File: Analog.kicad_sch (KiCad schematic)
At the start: 15 parts, among them J2 Conn_01x02_Socket, J3 Conn_01x02_Socket, U3 MAX98357A, U7 TLV172IDCK

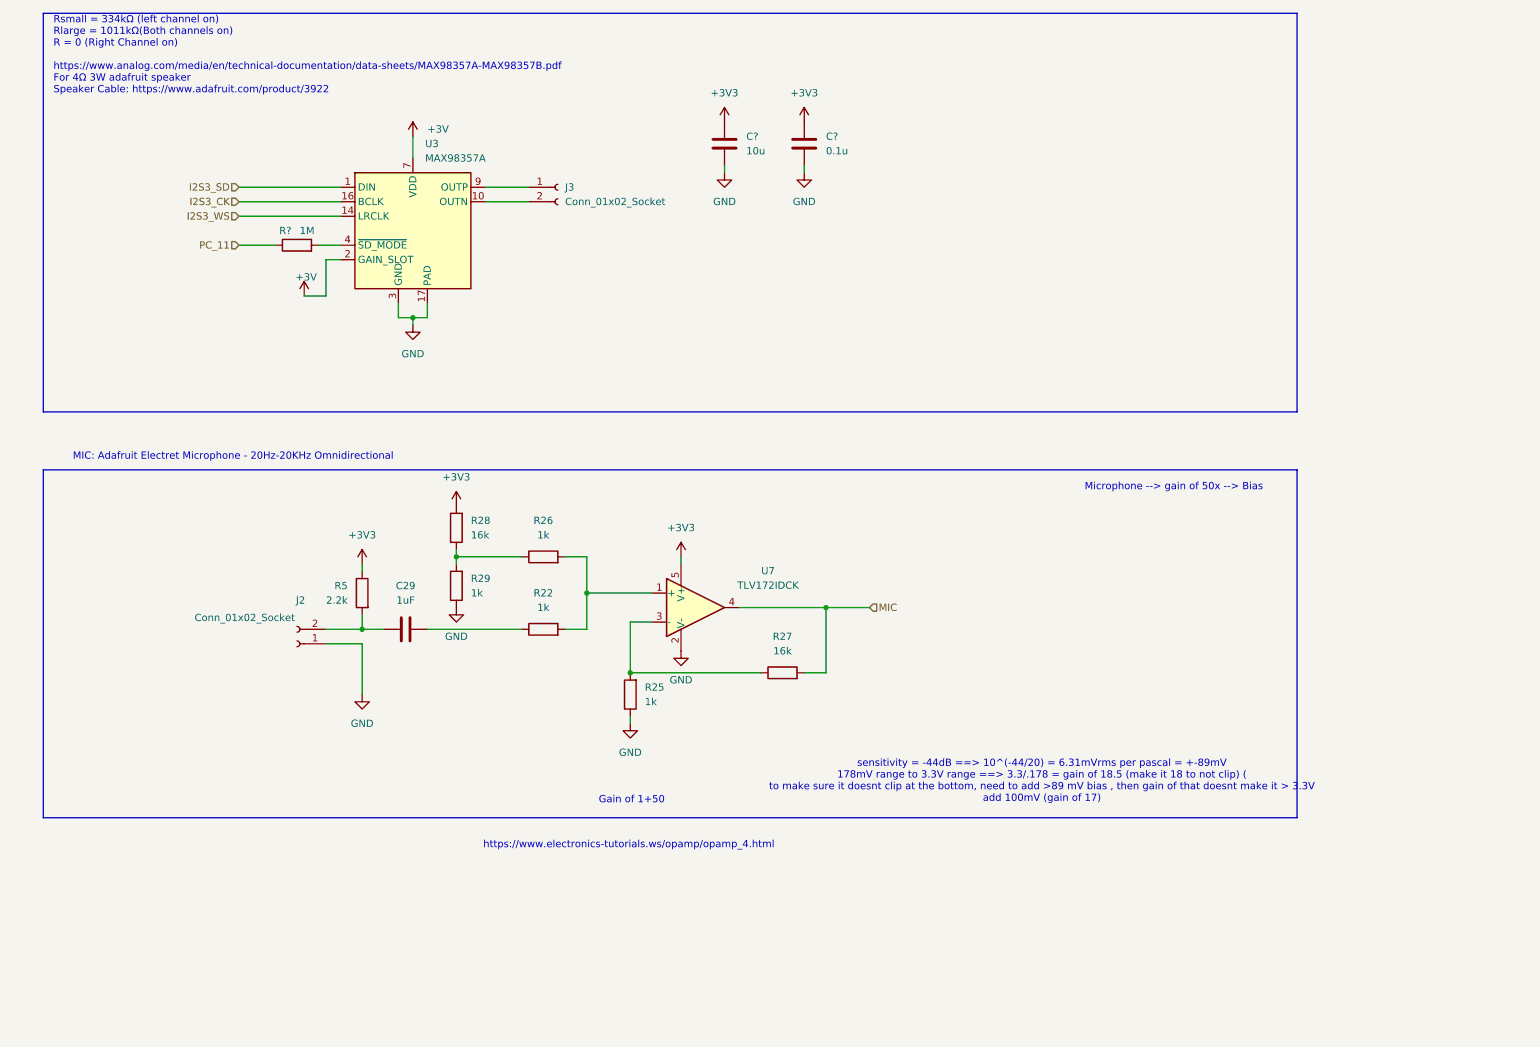
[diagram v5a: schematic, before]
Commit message: added charge pump, fixed analog audio
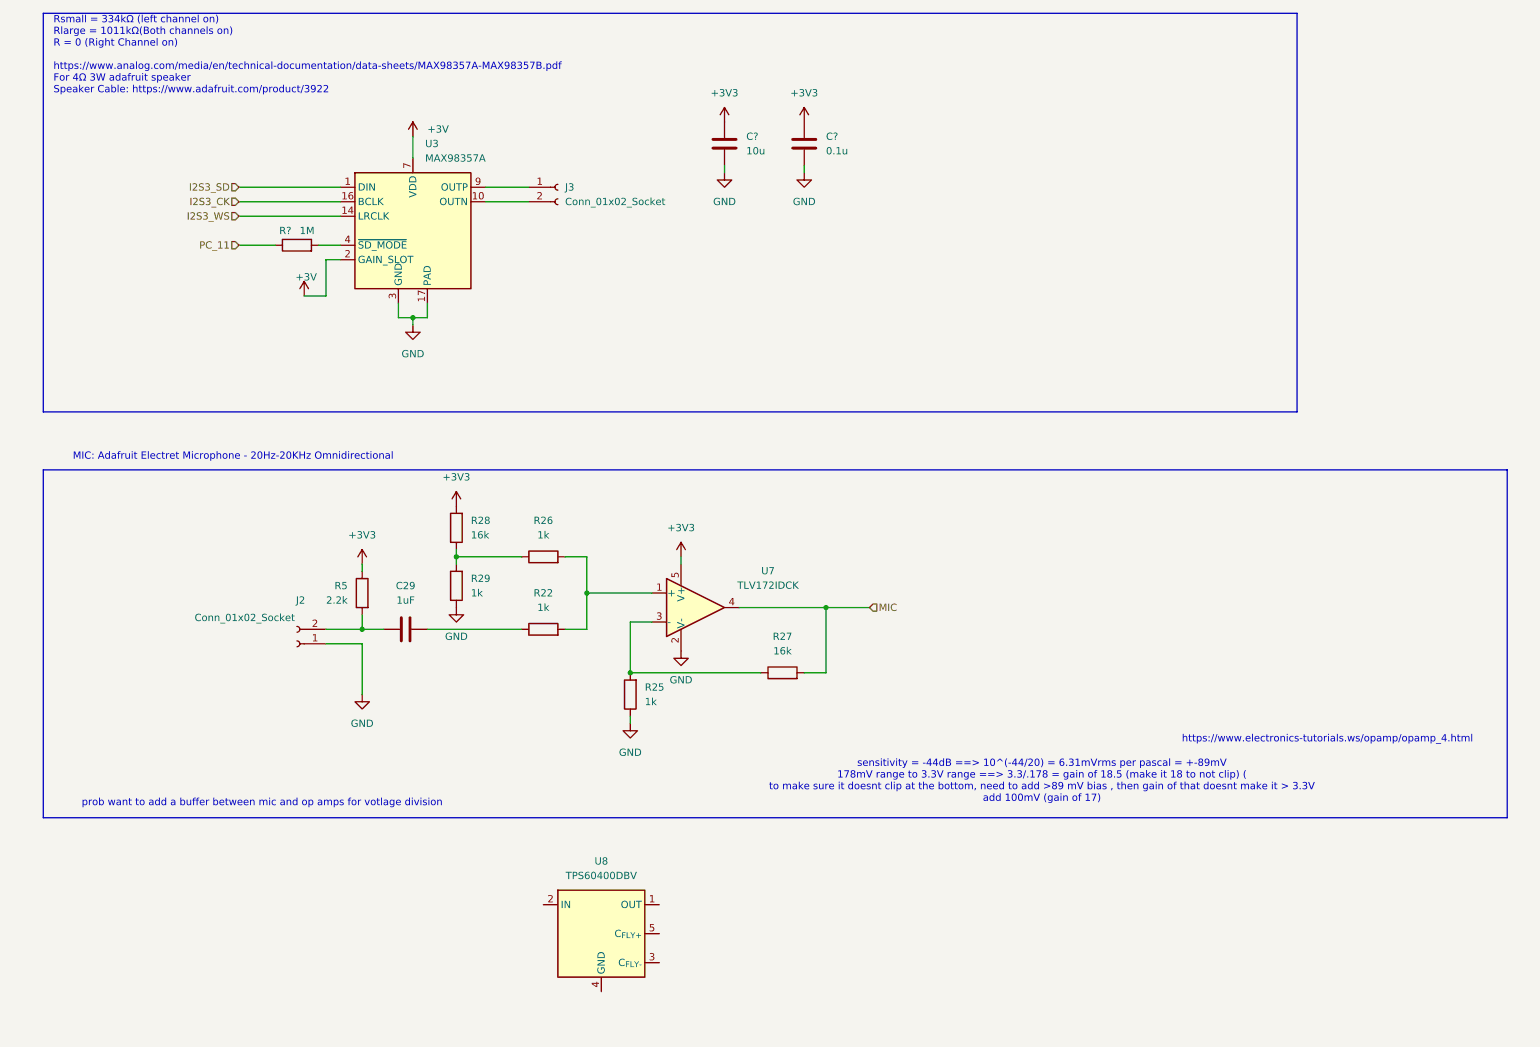
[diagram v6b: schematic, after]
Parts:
- added U8: TPS60400DBV, Package_TO_SOT_SMD:SOT-23-5, symbol Regulator_SwitchedCapacitor:TPS60400DBV
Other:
- note added: "prob want to add a buffer between mic and op amps for votlage division"
- note removed: "Gain of 1+50"
- note removed: "Microphone --> gain of 50x --> Bias"
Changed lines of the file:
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@@
 	(rectangle
 		(start 21.59 95.25)
-		(end 241.3 156.21)
+		(end 278.13 156.21)
 		(stroke
 			(width 0)
@@
 		)
 	)
-	(text "Microphone --> gain of 50x --> Bias"
-		(exclude_from_sim no)
-		(at 219.71 98.298 0)
-		(effects
-			(font
-				(size 1.27 1.27)
-			)
-		)
-	)
 	(text "sensitivity = -44dB ==> 10^(-44/20) = 6.31mVrms per pascal = +-89mV\n178mV range to 3.3V range ==> 3.3/.178 = gain of 18.5 (make it 18 to not clip) (\nto make sure it doesnt clip at the bottom, need to add >89 mV bias , then gain of that doesnt make it > 3.3V\nadd 100mV (gain of 17)\n\n"
 		(exclude_from_sim no)
@@
 	(text "https://www.electronics-tutorials.ws/opamp/opamp_4.html\n"
 		(exclude_from_sim no)
-		(at 124.206 161.036 0)
+		(at 246.634 142.494 0)
 		(effects
 			(font
@@
 		)
 	)
-	(text "Gain of 1+50\n"
+	(text "prob want to add a buffer between mic and op amps for votlage division\n"
 		(exclude_from_sim no)
-		(at 124.714 153.162 0)
+		(at 59.944 153.67 0)
 		(effects
 			(font
@@
 	)
 	(image
-		(at 104.14 180.34)
+		(at 52.07 172.72)
 		(scale 0.229285)
 		(data "iVBORw0KGgoAAAANSUhEUgAABeQAAAJCCAYAAACh2scVAAAMP2lDQ1BJQ0MgUHJvZmlsZQAASImV"
@@
 	)
 	(image
-		(at 44.45 177.8)
+		(at 252.73 128.27)
 		(scale 0.213501)
 		(data "iVBORw0KGgoAAAANSUhEUgAABOAAAAI0CAYAAAC0xFZzAAAMP2lDQ1BJQ0MgUHJvZmlsZQAASImV"
@@
 	)
 	(image
-		(at 246.38 113.03)
-		(scale 0.415251)
+		(at 240.57 105.3291)
+		(scale 0.38707)
 		(data "iVBORw0KGgoAAAANSUhEUgAABCYAAAEKCAYAAADO/VTVAAAMP2lDQ1BJQ0MgUHJvZmlsZQAASImV"
 			"VwdYU8kWnltSIbQAAlJCb4KAlABSQmih92YjJAFCiTEQVOxlUcG1iwrY0FURBSsgdkSxsCj2vlhQ"
@@
 					(unit 1)
 				)
+			)
+		)
+	)
+	(symbol
+		(lib_id "Regulator_SwitchedCapacitor:TPS60400DBV")
+		(at 119.38 176.53 0)
+		(unit 1)
+		(body_style 1)
+		(exclude_from_sim no)
+		(in_bom yes)
+		(on_board yes)
+		(in_pos_files yes)
+		(dnp no)
+		(fields_autoplaced yes)
+		(property "Reference" "U8"
+			(at 119.38 163.83 0)
+			(show_name no)
+			(do_not_autoplace no)
+			(effects
+				(font
+					(size 1.27 1.27)
+				)
+			)
+		)
+		(property "Value" "TPS60400DBV"
+			(at 119.38 166.37 0)
+			(show_name no)
+			(do_not_autoplace no)
+			(effects
+				(font
+					(size 1.27 1.27)
+				)
+			)
+		)
+		(property "Footprint" "Package_TO_SOT_SMD:SOT-23-5"
+			(at 119.38 163.83 0)
+			(hide yes)
+			(show_name no)
+			(do_not_autoplace no)
+			(effects
+				(font
+					(size 1.27 1.27)
+				)
+			)
+		)
+		(property "Datasheet" "https://www.ti.com/lit/ds/symlink/tps60400.pdf"
+			(at 119.38 199.39 0)
+			(hide yes)
+			(show_name no)
+			(do_not_autoplace no)
+			(effects
+				(font
+					(size 1.27 1.27)
+				)
+			)
+		)
+		(property "Description" "Unregulated 60-mA Charge Pump Voltage Inverter with Variable Switching Frequency 50 kHz - 250 kHz, SOT-23-5"
+			(at 119.38 176.53 0)
+			(hide yes)
+			(show_name no)
+			(do_not_autoplace no)
+			(effects
+				(font
+					(size 1.27 1.27)
+				)
+			)
+		)
+		(pin "1"
+		)
+		(pin "5"
+		)
+		(pin "4"
+		)
+		(pin "3"
+		)
+		(pin "2"
+		)
+		(instances
+			(project "SeniorDesign_PCB"
+				(path "/88e1ced0-9576-4565-ab29-f74bf51ccbda/f9ef2c8a-940c-4bd3-9d49-5676059e2f63"
+					(reference "U8")
+					(unit 1)
+				)

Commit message: added second audio dac
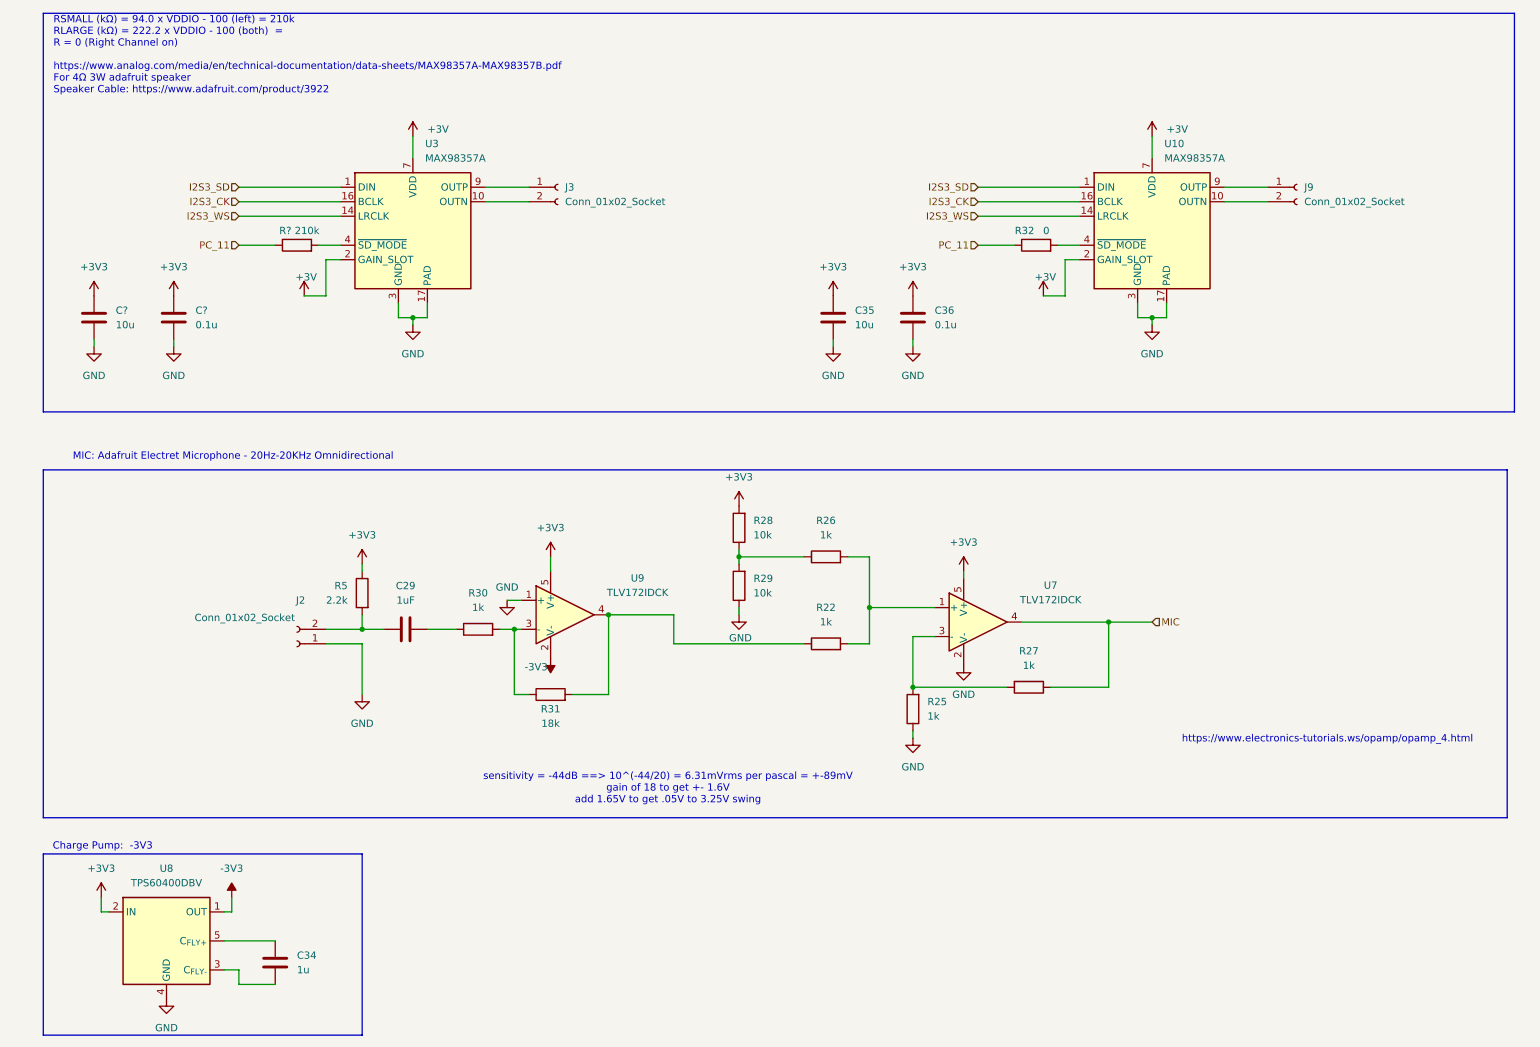
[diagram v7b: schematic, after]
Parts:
- added C34: 1u, Package_TO_SOT_SMD:SOT-23-5, symbol Device:C
- added C35: 10u, Capacitor_SMD:C_0603_1608Metric, symbol Device:C
- added C36: 0.1u, Capacitor_SMD:C_0603_1608Metric, symbol Device:C
- added J9: Conn_01x02_Socket, symbol Connector:Conn_01x02_Socket
- added R30: 1k, Resistor_SMD:R_0603_1608Metric, symbol Device:R
- added R31: 18k, Resistor_SMD:R_0603_1608Metric, symbol Device:R
- added R32: 0, Resistor_SMD:R_0603_1608Metric, symbol Device:R
- added U10: MAX98357A, Package_DFN_QFN:TQFN-16-1EP_3x3mm_P0.5mm_EP1.23x1.23mm, symbol Audio:MAX98357A
- added U9: TLV172IDCK, Package_TO_SOT_SMD:SOT-353_SC-70-5, symbol Amplifier_Operational:TLV172IDCK
- R27: value 16k -> 1k
- R28: value 16k -> 10k
- R29: value 1k -> 10k
- R?: value 1M -> 210k
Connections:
- net +3V: now also U10.2 (GAIN_SLOT), U10.7 (VDD), U10.8 (VDD)
- net +3V3: now also U8.2 (IN), C35.1, C36.1, U9.5 (V+)
- net GND: now also U8.4 (GND), C35.2, C36.2, U10.11 (GND), U10.15 (GND), U10.17 (PAD), U10.3 (GND), U9.1 (+)
- net I2S3_CK: now also U10.16 (BCLK)
- net I2S3_SD: now also U10.1 (DIN)
- net I2S3_WS: now also U10.14 (LRCLK)
- net MIC: now also R27.1; no longer R27.2
- net PC_11: now also R32.1
- net at R22.1: now also R31.2, U9.4; no longer C29.1
- net -3V3: now reaches U8.1 (OUT)
- net -3V3: now also U9.2 (V-)
- net at U8.3 (C_{FLY-}): now also C34.2
- net at U8.5 (C_{FLY+}): now also C34.1
- net at R25.2, U7.3 (-): now also R27.2; no longer R27.1
- new net: J9.2 (Pin_2), U10.10 (OUTN)
- new net: R32.2, U10.4 (~{SD_MODE})
- new net: J9.1 (Pin_1), U10.9 (OUTP)
- new net: R30.2, R31.1, U9.3 (-)
- new net: C29.1, R30.1
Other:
- note added: "Charge Pump: -3V3"
- note added: "RSMALL (kΩ) = 94.0 x VDDIO - 100 (left) = 210k RLARGE (kΩ) = 222.2 x VDDIO - 100 (both) = R = 0 (Right Channel on) https://www.analog.com/media/en/technical-documentation/data-sheets/MAX98357A-MAX98357B.pdf For 4Ω 3W adafruit speaker Speaker Cable: https://www.adafruit.com/product/3922"
- note added: "sensitivity = -44dB ==> 10^(-44/20) = 6.31mVrms per pascal = +-89mV gain of 18 to get +- 1.6V add 1.65V to get .05V to 3.25V swing"
- note removed: "Rsmall = 334kΩ (left channel on) Rlarge = 1011kΩ(Both channels on) R = 0 (Right Channel on) https://www.analog.com/media/en/technical-documentation/data-sheets/MAX98357A-MAX98357B.pdf For 4Ω 3W adafruit speaker Speaker Cable: https://www.adafruit.com/product/3922"
- note removed: "prob want to add a buffer between mic and op amps for votlage division"
- note removed: "sensitivity = -44dB ==> 10^(-44/20) = 6.31mVrms per pascal = +-89mV 178mV range to 3.3V range ==> 3.3/.178 = gain of 18.5 (make it 18 to not clip) ( to make sure it doesnt clip at the bottom, need to add >89 mV bias , then gain of that doesnt make it > 3.3V add 100mV (gain of 17)"
- moved on the sheet: C?, R22, R25, R26, R28, R29, U7, U8

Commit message: block diagram, added flyback on LED
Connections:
- net PC_11 renamed SD_MODE
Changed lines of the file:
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@@
 		)
 	)
-	(hierarchical_label "PC_11"
+	(hierarchical_label "SD_MODE"
 		(shape input)
 		(at 55.88 55.88 180)
@@
 		)
 	)
-	(hierarchical_label "PC_11"
+	(hierarchical_label "SD_MODE"
 		(shape input)
 		(at 185.42 55.88 180)
